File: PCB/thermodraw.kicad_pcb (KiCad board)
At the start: 2 copper layers, 26 parts, among them CON1 BARREL_JACK, J1 CONN-10-DIL, P1 Molex 47053-1000, Q1 DMP3098L, Q2 DMP3098L, Q3 DMP3098L, U1 TPS71533DCKR, U3 MKL05Z32VLC4

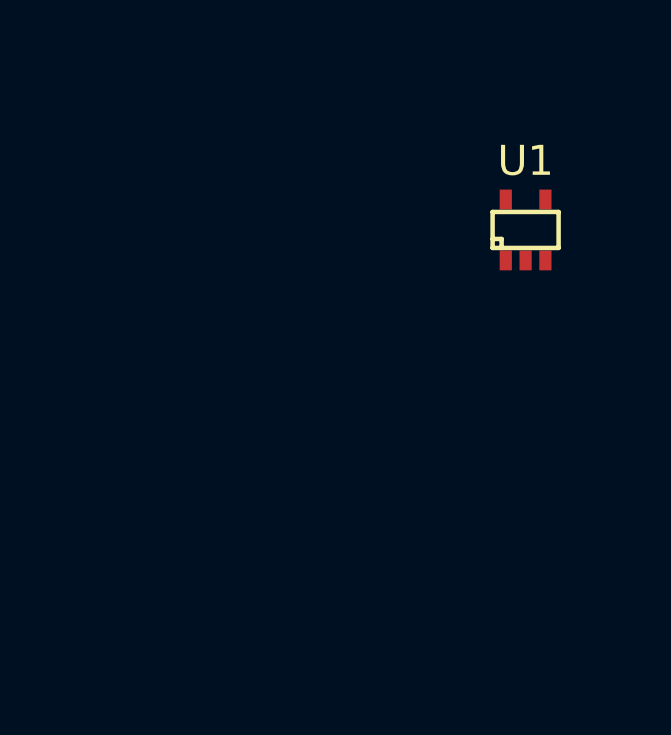
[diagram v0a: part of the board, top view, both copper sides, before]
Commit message: Added capacitor footprints.
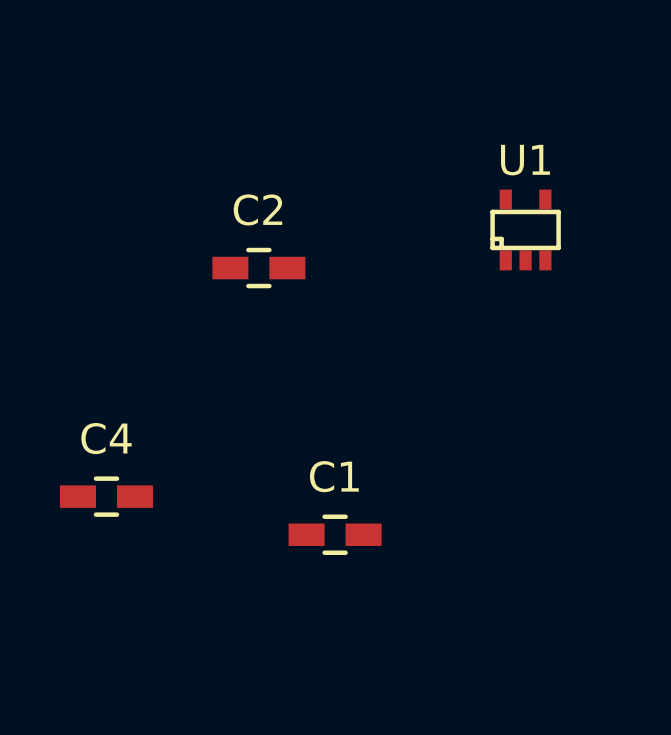
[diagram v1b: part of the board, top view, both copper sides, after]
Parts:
- added C1: 100 nF, Capacitors_SMD:C_0603_HandSoldering, F.Cu at (108.0, 97.8)
- added C2: 470 nF, Capacitors_SMD:C_0603_HandSoldering, F.Cu at (105.4, 88.9)
- added C4: 470 nF, Capacitors_SMD:C_0603_HandSoldering, F.Cu at (100.3, 96.5)
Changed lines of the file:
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@@
 (kicad_pcb (version 4) (host pcbnew 4.0.4+dfsg1-stable)
   (general
-    (links 69)
-    (no_connects 69)
+    (links 75)
+    (no_connects 72)
     (area 0 0 0 0)
     (thickness 1.6)
@@
     (tracks 0)
     (zones 0)
-    (modules 26)
+    (modules 29)
     (nets 53)
   )
@@
       (net 21 /SWDIO/TMS))
   )
+  (module Capacitors_SMD:C_0603_HandSoldering (layer F.Cu)
+    (at 107.95 97.79)
+    (descr "Capacitor SMD 0603, hand soldering")
+    (tags "capacitor 0603")
+    (attr smd)
+    (fp_text reference C1 (at 0 -1.9) (layer F.SilkS)
+      (effects (font (size 1 1) (thickness 0.15)))
+    )
+    (fp_text value "100 nF" (at 0 1.9) (layer F.Fab)
+      (effects (font (size 1 1) (thickness 0.15)))
+    )
+    (fp_line (start -1.85 -0.75) (end 1.85 -0.75) (layer F.CrtYd) (width 0.05))
+    (fp_line (start -1.85 0.75) (end 1.85 0.75) (layer F.CrtYd) (width 0.05))
+    (fp_line (start -1.85 -0.75) (end -1.85 0.75) (layer F.CrtYd) (width 0.05))
+    (fp_line (start 1.85 -0.75) (end 1.85 0.75) (layer F.CrtYd) (width 0.05))
+    (fp_line (start -0.35 -0.6) (end 0.35 -0.6) (layer F.SilkS) (width 0.15))
+    (fp_line (start 0.35 0.6) (end -0.35 0.6) (layer F.SilkS) (width 0.15))
+    (pad 1 smd rect (at -0.95 0) (size 1.2 0.75) (layers F.Cu F.Paste F.Mask)
+      (net 12 +12V))
+    (pad 2 smd rect (at 0.95 0) (size 1.2 0.75) (layers F.Cu F.Paste F.Mask)
+      (net 13 GND))
+    (model Capacitors_SMD.3dshapes/C_0603_HandSoldering.wrl
+      (at (xyz 0 0 0))
+      (scale (xyz 1 1 1))
+      (rotate (xyz 0 0 0))
+    )
+  )
+  (module Capacitors_SMD:C_0603_HandSoldering (layer F.Cu)
+    (at 105.41 88.9)
+    (descr "Capacitor SMD 0603, hand soldering")
+    (tags "capacitor 0603")
+    (attr smd)
+    (fp_text reference C2 (at 0 -1.9) (layer F.SilkS)
+      (effects (font (size 1 1) (thickness 0.15)))
+    )
+    (fp_text value "470 nF" (at 0 1.9) (layer F.Fab)
+      (effects (font (size 1 1) (thickness 0.15)))
+    )
+    (fp_line (start -1.85 -0.75) (end 1.85 -0.75) (layer F.CrtYd) (width 0.05))
+    (fp_line (start -1.85 0.75) (end 1.85 0.75) (layer F.CrtYd) (width 0.05))
+    (fp_line (start -1.85 -0.75) (end -1.85 0.75) (layer F.CrtYd) (width 0.05))
+    (fp_line (start 1.85 -0.75) (end 1.85 0.75) (layer F.CrtYd) (width 0.05))
+    (fp_line (start -0.35 -0.6) (end 0.35 -0.6) (layer F.SilkS) (width 0.15))
+    (fp_line (start 0.35 0.6) (end -0.35 0.6) (layer F.SilkS) (width 0.15))
+    (pad 1 smd rect (at -0.95 0) (size 1.2 0.75) (layers F.Cu F.Paste F.Mask)
+      (net 12 +12V))
+    (pad 2 smd rect (at 0.95 0) (size 1.2 0.75) (layers F.Cu F.Paste F.Mask)
+      (net 13 GND))
+    (model Capacitors_SMD.3dshapes/C_0603_HandSoldering.wrl
+      (at (xyz 0 0 0))
+      (scale (xyz 1 1 1))
+      (rotate (xyz 0 0 0))
+    )
+  )
+  (module Capacitors_SMD:C_0603_HandSoldering (layer F.Cu)
+    (at 100.33 96.52)
+    (descr "Capacitor SMD 0603, hand soldering")
+    (tags "capacitor 0603")
+    (attr smd)
+    (fp_text reference C4 (at 0 -1.9) (layer F.SilkS)
+      (effects (font (size 1 1) (thickness 0.15)))
+    )
+    (fp_text value "470 nF" (at 0 1.9) (layer F.Fab)
+      (effects (font (size 1 1) (thickness 0.15)))
+    )
+    (fp_line (start -1.85 -0.75) (end 1.85 -0.75) (layer F.CrtYd) (width 0.05))
+    (fp_line (start -1.85 0.75) (end 1.85 0.75) (layer F.CrtYd) (width 0.05))
+    (fp_line (start -1.85 -0.75) (end -1.85 0.75) (layer F.CrtYd) (width 0.05))
+    (fp_line (start 1.85 -0.75) (end 1.85 0.75) (layer F.CrtYd) (width 0.05))
+    (fp_line (start -0.35 -0.6) (end 0.35 -0.6) (layer F.SilkS) (width 0.15))
+    (fp_line (start 0.35 0.6) (end -0.35 0.6) (layer F.SilkS) (width 0.15))
+    (pad 1 smd rect (at -0.95 0) (size 1.2 0.75) (layers F.Cu F.Paste F.Mask)
+      (net 17 VDD))
+    (pad 2 smd rect (at 0.95 0) (size 1.2 0.75) (layers F.Cu F.Paste F.Mask)
+      (net 13 GND))
+    (model Capacitors_SMD.3dshapes/C_0603_HandSoldering.wrl
+      (at (xyz 0 0 0))
+      (scale (xyz 1 1 1))
+      (rotate (xyz 0 0 0))
+    )
+  )
 )

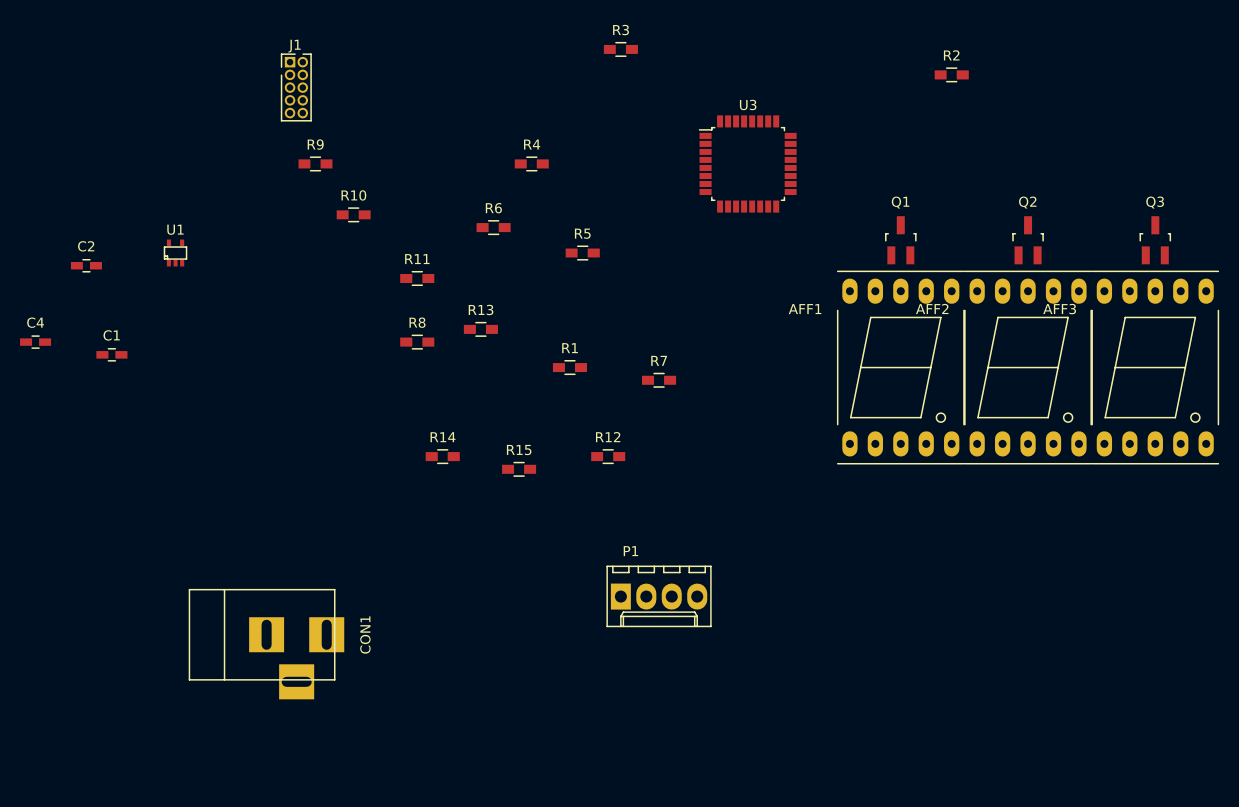
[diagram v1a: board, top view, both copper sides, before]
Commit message: Finished routing, added pours.
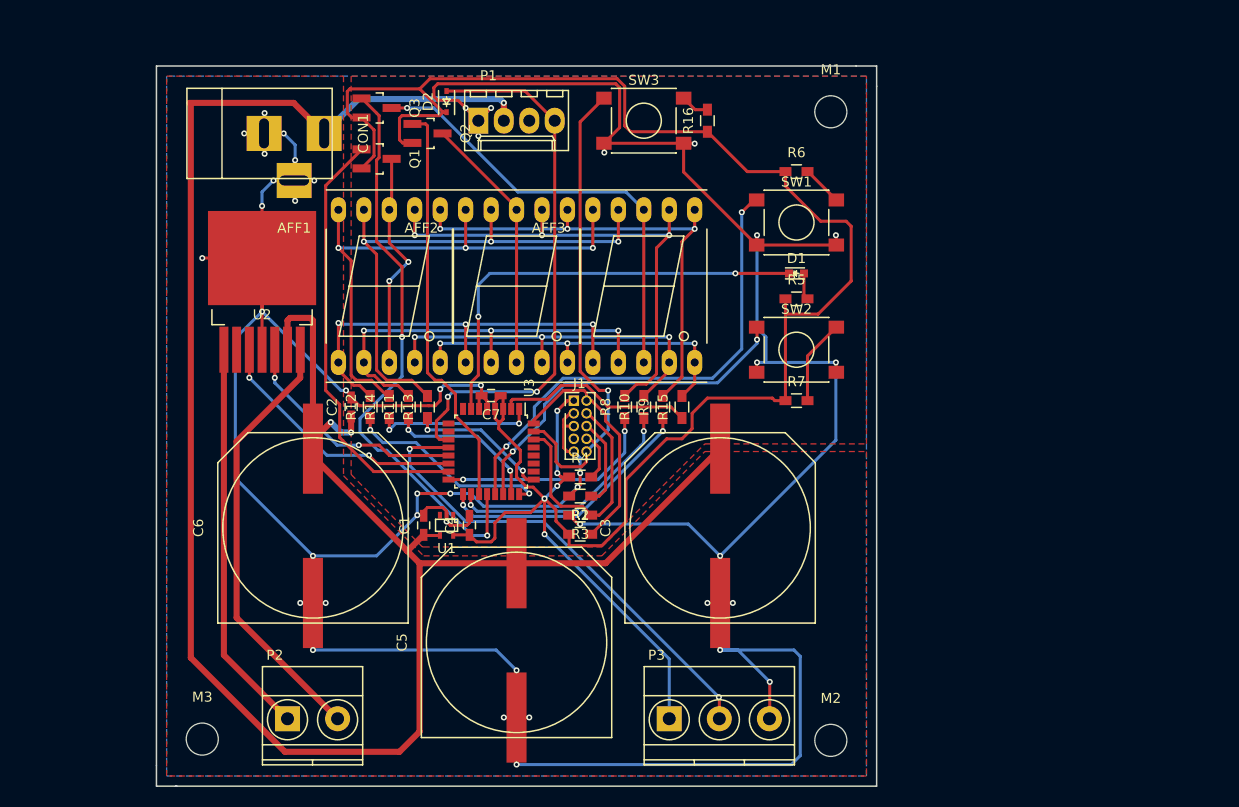
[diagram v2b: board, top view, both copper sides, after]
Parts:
- added C3: 1500 uF, Custom:c_elec_18x22, F.Cu at (168.7, 115.1)
- added C5: 1500 uF, Custom:c_elec_18x22, F.Cu at (148.3, 126.5)
- added C6: 1500 uF, Custom:c_elec_18x22, F.Cu at (128.0, 115.1)
- added C7: 100 nF, Capacitors_SMD:C_0603_HandSoldering, F.Cu at (145.8, 101.9)
- added D1: SET, LEDs:LED_0603, F.Cu at (176.3, 89.7)
- added D2: CUS520,H3F, Diodes_SMD:SOD-323, F.Cu at (141.4, 72.5)
- added M1: MountingHole_3.2mm_M3, Mounting_Holes:MountingHole_3.2mm_M3, F.Cu at (179.7, 73.5)
- added M2: MountingHole_3.2mm_M3, Mounting_Holes:MountingHole_3.2mm_M3, F.Cu at (179.7, 136.3)
- added M3: MountingHole_3.2mm_M3, Mounting_Holes:MountingHole_3.2mm_M3, F.Cu at (117.0, 136.1)
- added P2: CONN_01X02, Terminal_Blocks:TerminalBlock_Pheonix_MKDS1.5-2pol, F.Cu at (125.5, 134.1)
- added P3: CONN_01X03, Terminal_Blocks:TerminalBlock_Pheonix_MKDS1.5-3pol, F.Cu at (163.6, 134.1)
- added R16: 47k, Resistors_SMD:R_0603_HandSoldering, F.Cu at (167.4, 74.4)
- added SW1: T_UP, Buttons_Switches_SMD:SW_SPST_PTS645, F.Cu at (176.3, 84.6)
- added SW2: T_DOWN, Buttons_Switches_SMD:SW_SPST_PTS645, F.Cu at (176.3, 97.3)
- added SW3: RESET, Buttons_Switches_SMD:SW_SPST_PTS645, F.Cu at (161.0, 74.4)
- added U2: TLE52062G, Custom:TO-263-7Lead, F.Cu at (122.9, 97.3)
- moved Q3 78.8 mm to (134.4, 73.2), turned to 270 degrees
- moved Q2 60.9 mm to (139.4, 75.7), turned to 270 degrees
- moved R2 59.0 mm to (154.7, 115.7)
- moved Q1 53.0 mm to (134.4, 78.2), turned to 270 degrees
- moved AFF1 51.7 mm to (135.6, 90.9)
- moved AFF3 51.7 mm to (161.0, 90.9)
- moved AFF2 51.7 mm to (148.3, 90.9)
- moved CON1 50.0 mm to (122.9, 75.7)
- moved P1 49.6 mm to (144.5, 74.4)
- moved C4 47.0 mm to (143.6, 114.8), turned to 90 degrees
- moved R3 46.7 mm to (154.7, 113.8), turned to 180 degrees
- moved J1 44.1 mm to (154.1, 102.4)
- moved R9 42.3 mm to (162.9, 103.0), turned to 90 degrees
- moved U3 38.5 mm to (145.8, 107.4), turned to 270 degrees
- moved U1 38.3 mm to (141.4, 114.8), turned to 180 degrees
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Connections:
- net Net-(AFF1-Pad3) renamed /AN_1_PWR
- net Net-(AFF2-Pad3) renamed /AN_2_PWR
- net Net-(AFF3-Pad3) renamed /AN_3_PWR
- R5 pad 2: Net-(D1-Pad2) -> /SET_AN
- U3 pad 15: Net-(U3-Pad15) -> /AN_1
- U3 pad 19: Net-(U3-Pad19) -> /AN_2
- U3 pad 20: Net-(U3-Pad20) -> /AN_3
- U3 pad 4: Net-(U3-Pad4) -> VDD
- U3 pad 5: Net-(U3-Pad5) -> GND
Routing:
- net GND: track 0.00 -> 406.4 mm, vias 0 -> 43
- net +12V: track 0.00 -> 216.2 mm, vias 0 -> 3
- net VDD: track 0.00 -> 211.0 mm, vias 0 -> 5
- net /AN_3: track 0.00 -> 58.1 mm, vias 0 -> 2
- net /SEG_G: track 0.00 -> 54.7 mm, vias 0 -> 3
- net /SW_FAN: track 0.00 -> 54.7 mm, vias 0 -> 2
- net /SEG_F: track 0.00 -> 54.4 mm, vias 0 -> 3
- net /T_UP: track 0.00 -> 53.1 mm, vias 0 -> 2
- net /SEG_A: track 0.00 -> 51.5 mm, vias 0 -> 3
- net /RESET: track 0.00 -> 50.7 mm, vias 0 -> 1
- net /SEG_B: track 0.00 -> 49.1 mm, vias 0 -> 3
- net /T_DATA: track 0.00 -> 48.2 mm, vias 0 -> 2
- net /AN_3_PWR: track 0.00 -> 44.6 mm, vias 0 -> 1
- net /T_DOWN: track 0.00 -> 44.5 mm, vias 0 -> 2
- net /SW_SET: track 0.00 -> 44.2 mm, vias 0 -> 2
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- added copper zone on F.Cu, net +12V
- added copper zone on B.Cu, net GND
- added copper zone on F.Cu, net GND
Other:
- board outline added: 71.9 x 71.9 mm
- net class Broad added: clearance 0.1524, trace_width 0.6096, via_dia 0.6, via_drill 0.3
- net class Default: clearance 0.2 -> 0.1524; trace_width 0.25 -> 0.3048; via_drill 0.4 -> 0.3
- net class Narrow added: clearance 0.1524, trace_width 0.1524, via_dia 0.6, via_drill 0.3
- rule trace_clearance: 0.2 -> 0.1524
- rule trace_min: 0.2 -> 0.1524
- rule via_min_size: 0.4 -> 0.6
